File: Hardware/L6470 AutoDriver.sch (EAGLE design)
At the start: 38 parts, among them U1 L6470

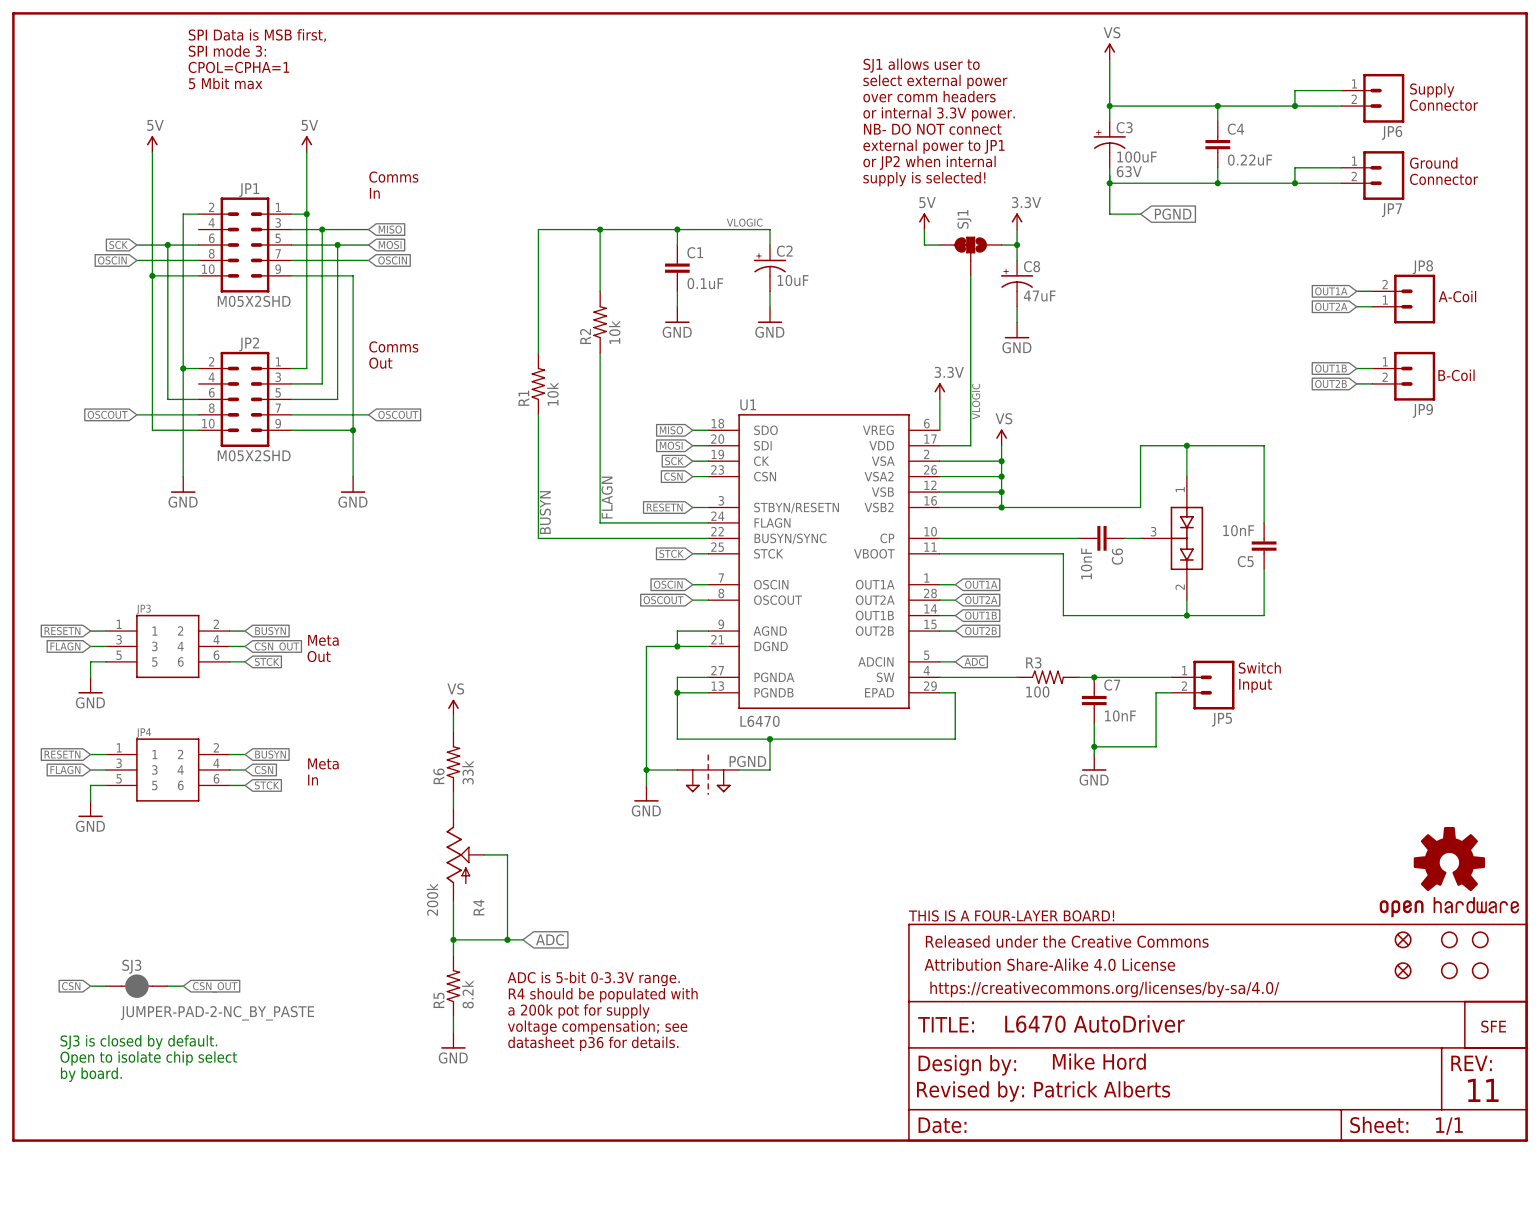
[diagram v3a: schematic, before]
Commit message: Making changes suggest by Pete L
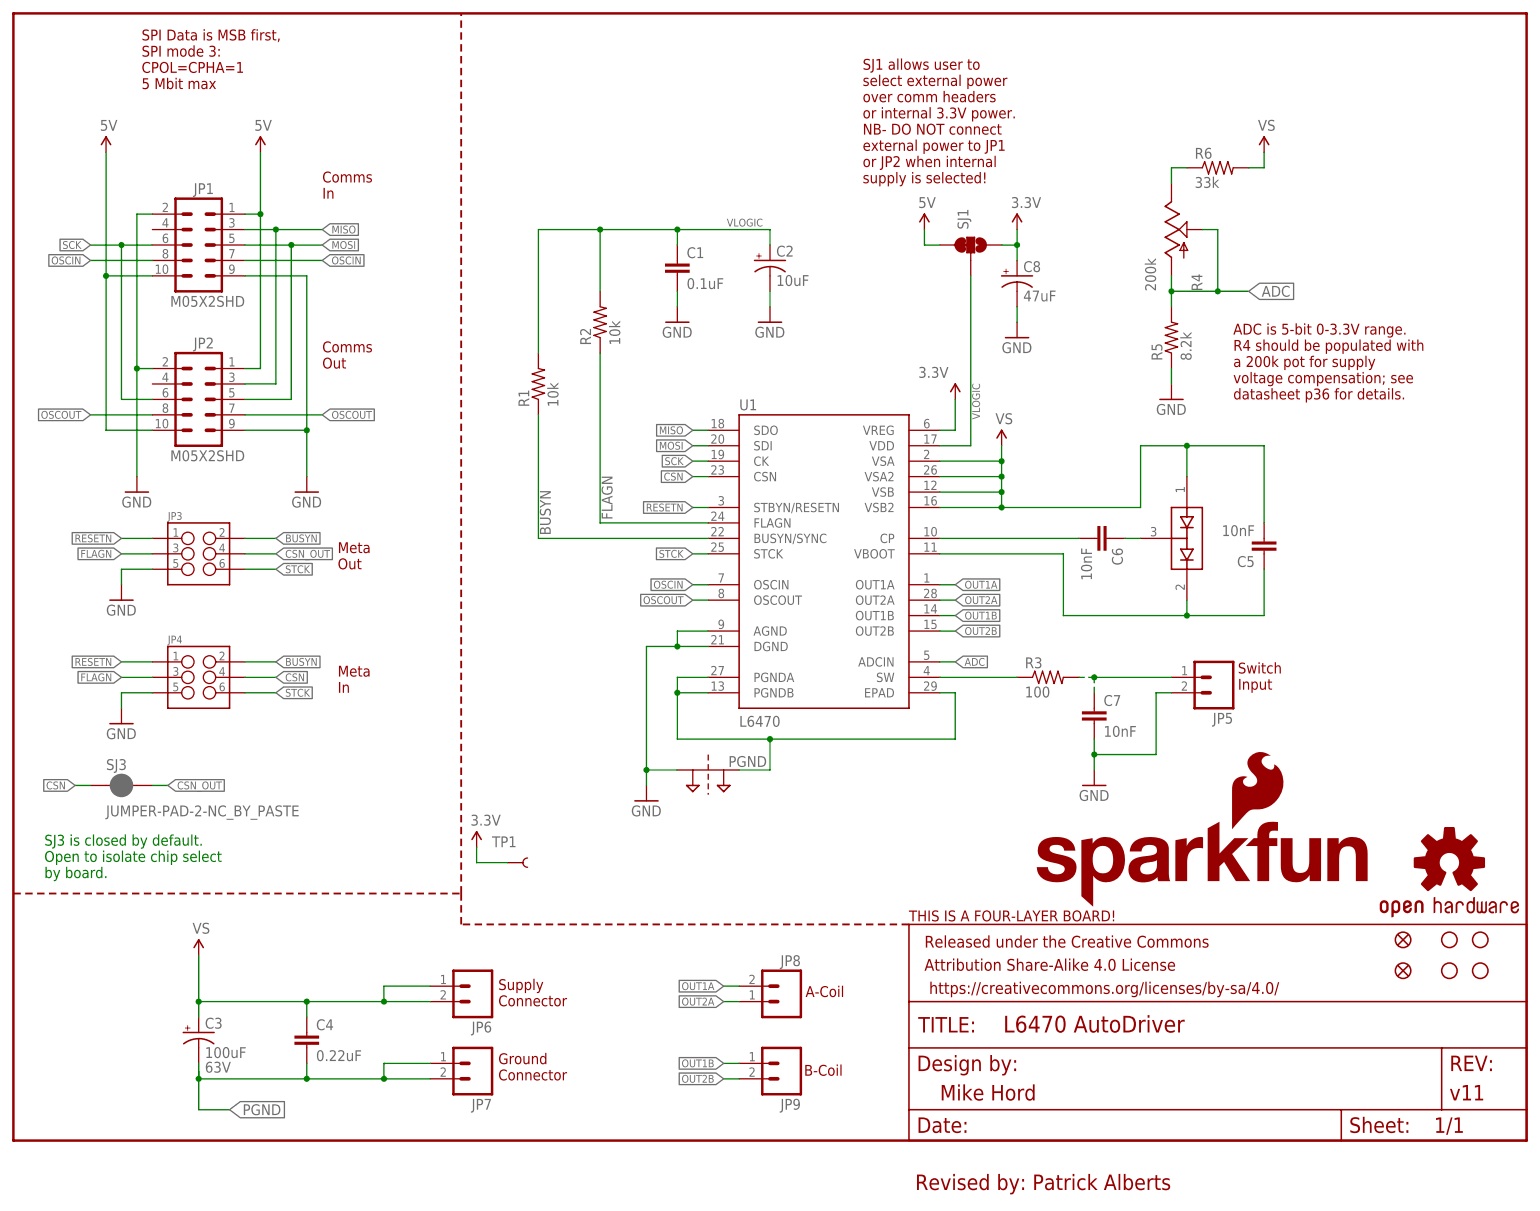
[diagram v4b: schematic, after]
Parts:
- added TP1: TEST-POINTTP_15TH_THRU, SparkFun-Passives:TEST-POINTTP_15TH_THRU
- C3: device SparkFun-Capacitors:CAP_POLD -> SparkFun-Capacitors:100UF-63V-20%(ELECT)
- FRAME1: value FRAME-LETTER -> (none); DESIGNER (none) -> Mike Hord; VERSION (none) -> v11
- JP3, JP4: device SparkFun-Connectors:M03X2 -> SparkFun-Connectors:M03X2SHROUD
- LOGO2: value LOGO-SFENEW -> SFE_LOGO_NAME_FLAME.2_INCH; device SparkFun:LOGO-SFENEW -> SparkFun-Aesthetics:SFE_LOGO_NAME_FLAME.2_INCH
- R4: device SparkFun:POT100K_3362U -> SparkFun-Electromechanical:POT100K_3362U
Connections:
- net 3.3V: now also TP1.1
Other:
- note removed: "11"
- note removed: "Mike Hord"
- moved on the sheet: C3, C4, C7, JP1, JP2, JP6, JP7, JP8, JP9, R4, R5, R6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

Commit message: Fixed more feedback from Pete after 1st proto cam failure
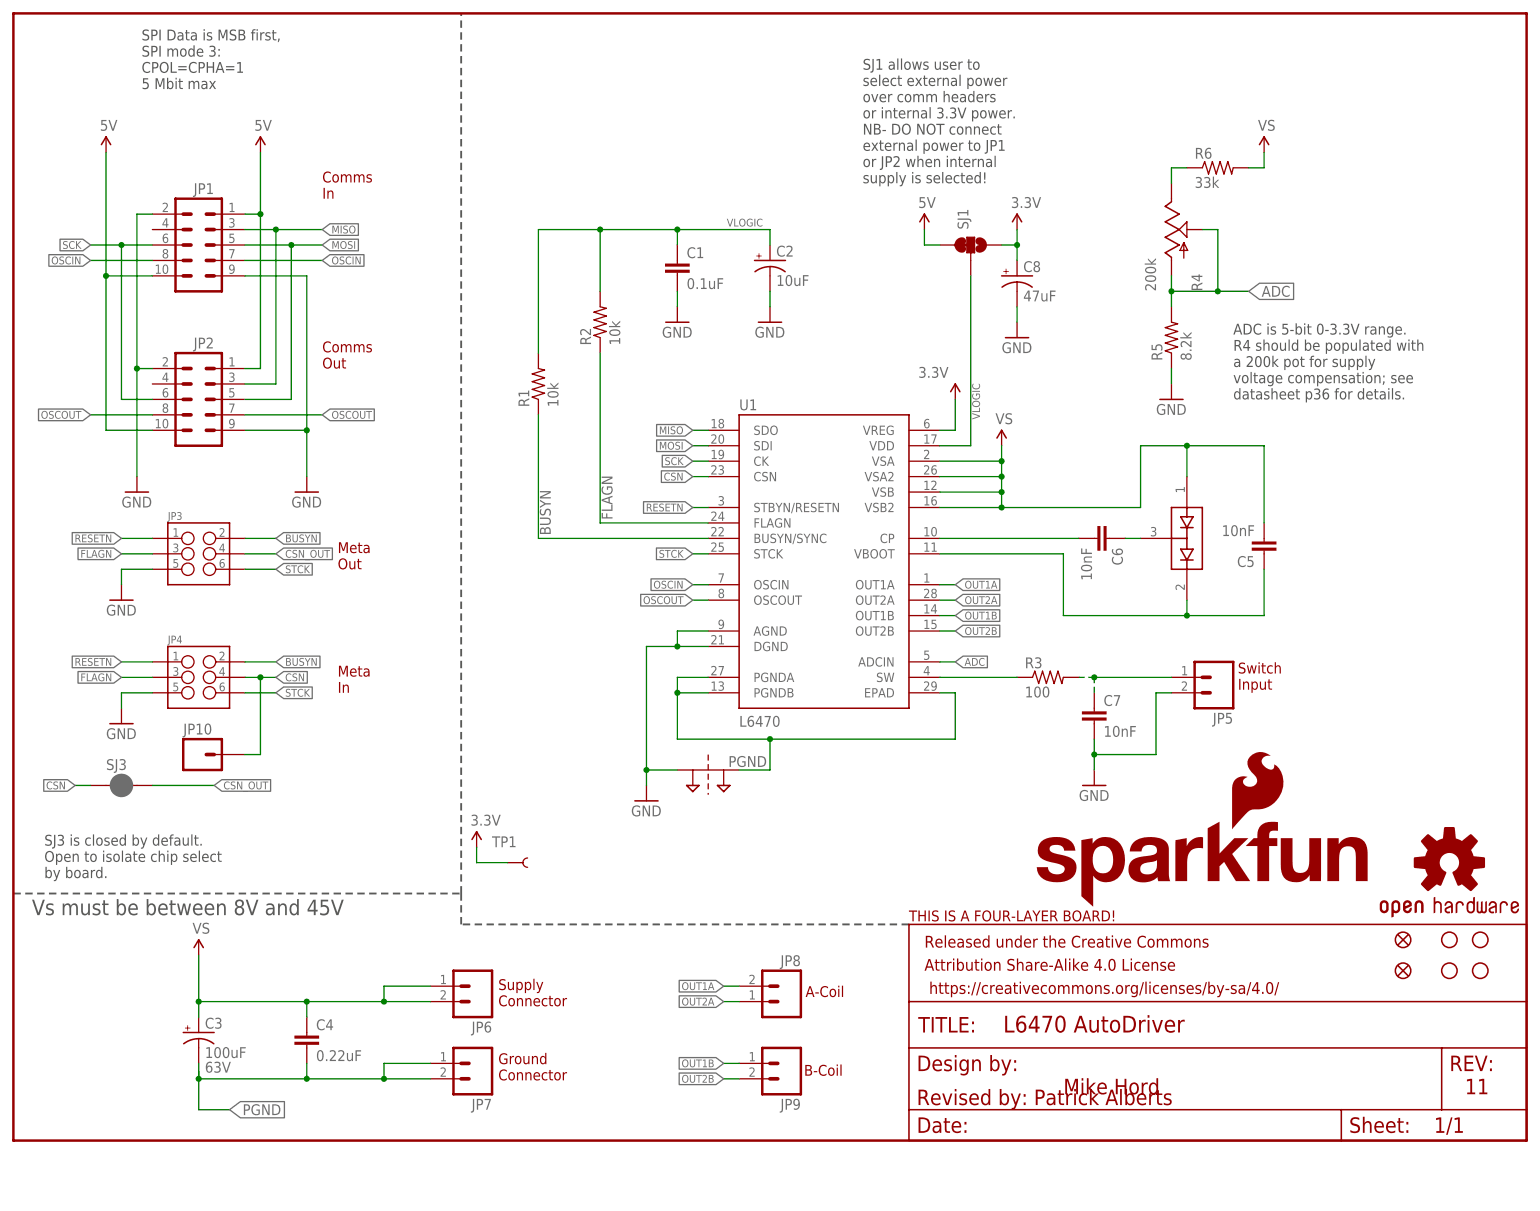
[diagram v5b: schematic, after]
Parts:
- added JP10: (no value), SparkFun-Connectors:M01PTH
- FRAME1: DESIGNER Mike Hord -> (none); VERSION v11 -> (none)
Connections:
- net CSN: now also JP10.1
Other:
- note added: "11"
- note added: "Mike Hord"
- note added: "Vs must be between 8V and 45V"

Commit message: Significant changes from customer feedback:  - now more daisy chainable  - labels changed to make more sense  - Change C5 to 220nF
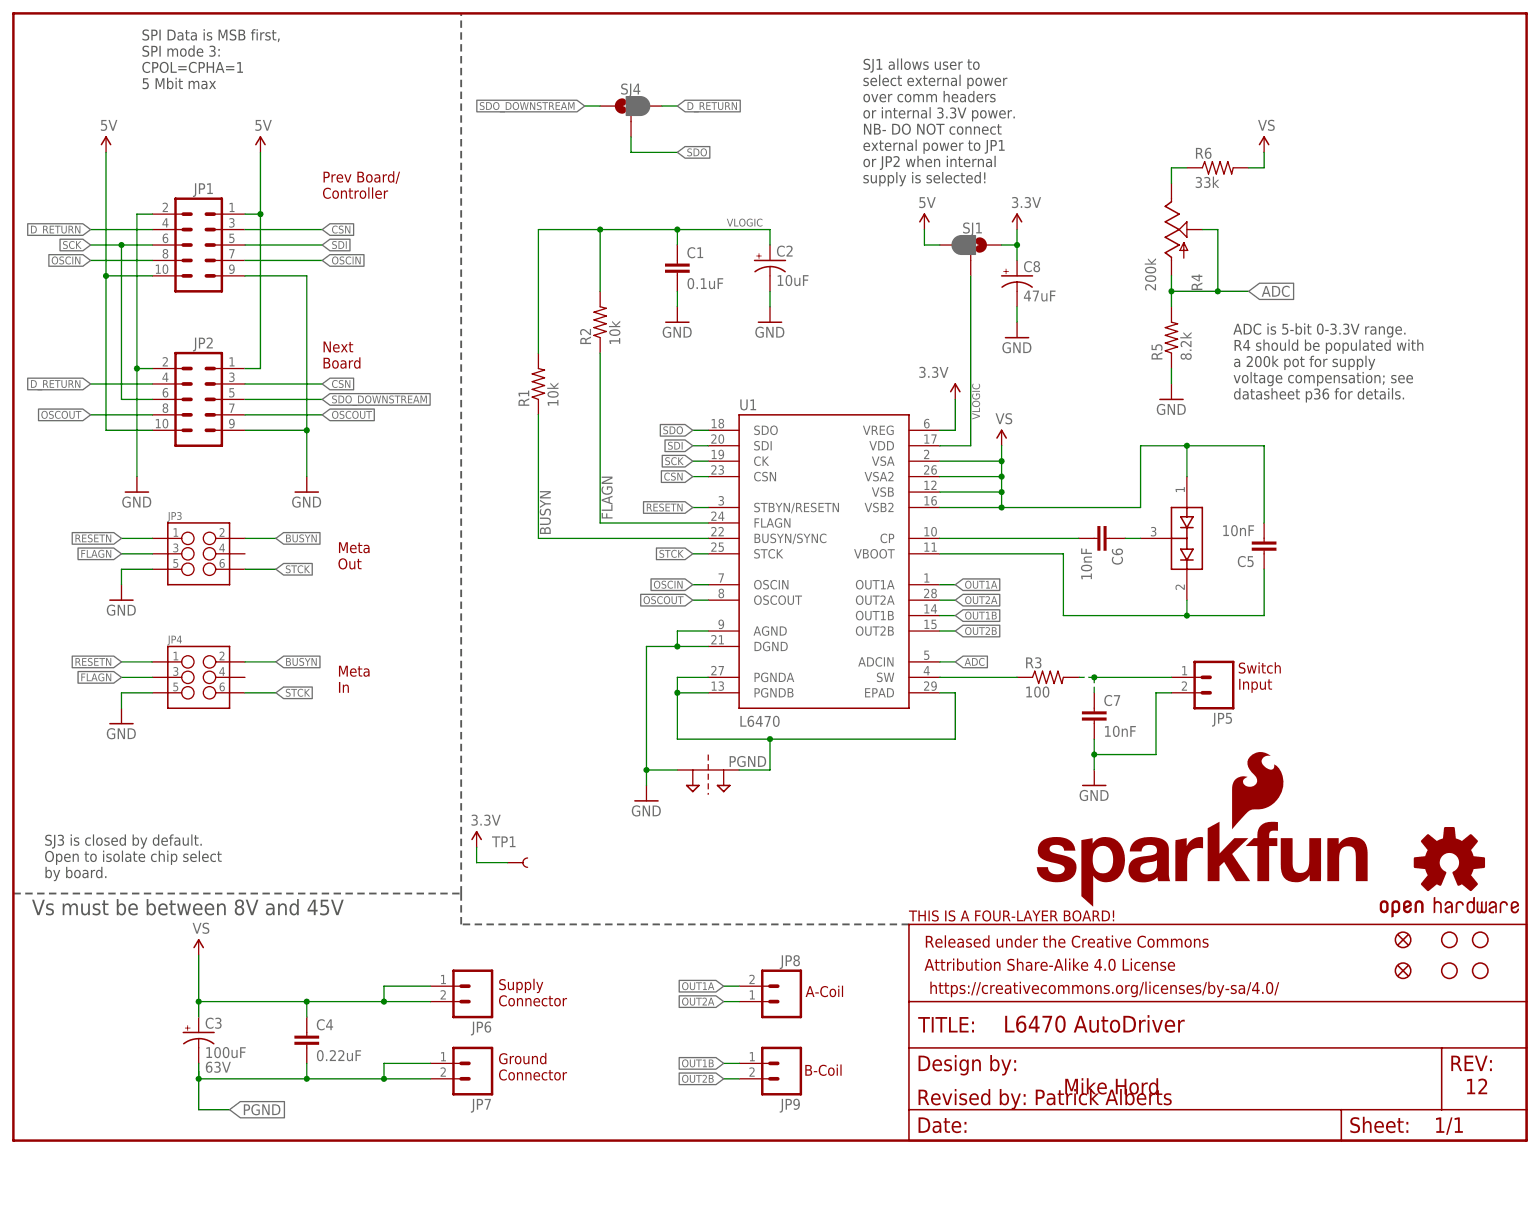
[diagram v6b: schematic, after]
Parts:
- removed JP10: (no value), SparkFun-Connectors:M01PTH
- removed SJ3: JUMPER-PAD-2-NC_BY_PASTE, SparkFun-Passives:JUMPER-PAD-2-NC_BY_PASTE
- added SJ4: JUMPER-PAD-3-2OF3_NC_BY_PASTE, SparkFun-Passives:JUMPER-PAD-3-2OF3_NC_BY_PASTE
- FRAME1: value (none) -> FRAME-LETTER
- SJ1: value (none) -> JUMPER-PAD-3-2OF3_NC_BY_PASTE; device SparkFun-Passives:SOLDERJUMPER_2WAYPASTE1&2 -> SparkFun-Passives:JUMPER-PAD-3-2OF3_NC_BY_PASTE
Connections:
- net N$5 renamed SWITCH_SIG
- net N$6 renamed SWITCH_INPUT
- net N$7 renamed V_CP
- net N$8 renamed CP_HIGH
- net N$9 renamed V_BOOT
- removed net CSN_OUT: JP3.4, SJ3.2
- removed net MISO: JP1.3, JP2.3, U1.SDO
- removed net MOSI: JP1.5, JP2.5, U1.SDI
- new net D_RETURN: JP1.4, JP2.4, SJ4.3
- new net SDI: JP1.5, U1.SDI
- new net SDO: SJ4.2, U1.SDO
- new net SDO_DOWNSTREAM: JP2.5, SJ4.1
- net 3.3V: now also SJ1.1; no longer SJ1.3
- net 5V: now also SJ1.3; no longer SJ1.1
- net CSN: now also JP1.3, JP2.3; no longer JP10.1, JP4.4, SJ3.1
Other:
- note added: "12"
- note added: "Next Board"
- note added: "Prev Board/ Controller"
- note removed: "11"
- note removed: "Comms In"
- note removed: "Comms Out"

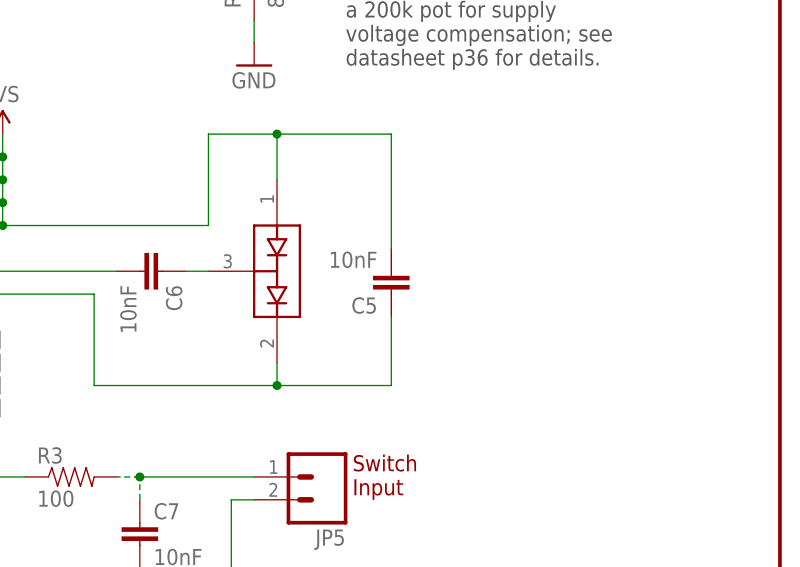
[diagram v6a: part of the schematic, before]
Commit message: Changes from customer feedback:  - now easier to daisy chain!  - labels make more sense in light of daisy chaining  - change C5 to 220nF
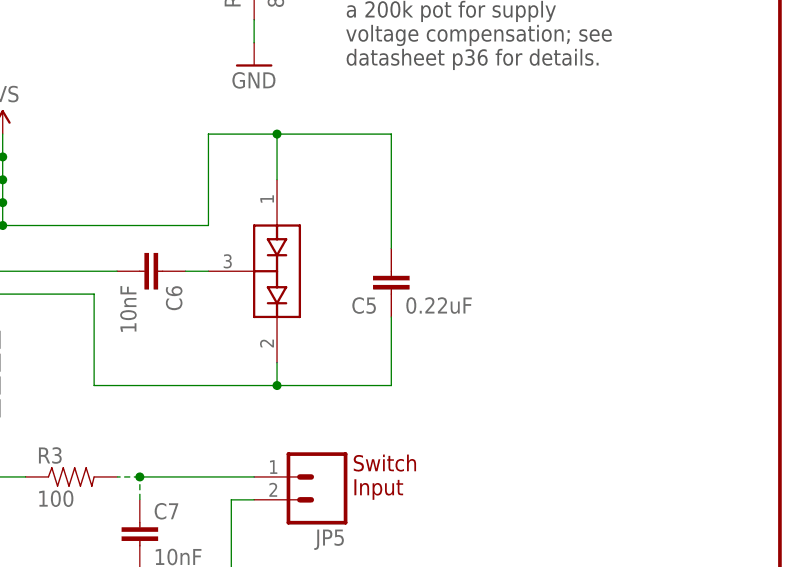
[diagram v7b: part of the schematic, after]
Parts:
- C5: value 10nF -> 0.22uF; device SparkFun-Capacitors:10NF/10000PF-50V-10%(0603) -> SparkFun-Capacitors:0.22UF50V-20%,+80%(0603)
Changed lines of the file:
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@@
 <part name="D1" library="SparkFun-DiscreteSemi" deviceset="BAV99" device="" value="BAV99"/>
 <part name="C6" library="SparkFun-Capacitors" deviceset="10NF/10000PF-50V-10%(0603)" device="" value="10nF"/>
-<part name="C5" library="SparkFun-Capacitors" deviceset="10NF/10000PF-50V-10%(0603)" device="" value="10nF"/>
+<part name="C5" library="SparkFun-Capacitors" deviceset="0.22UF50V-20%,+80%(0603)" device="" value="0.22uF"/>
 <part name="C4" library="SparkFun-Capacitors" deviceset="0.22UF50V-20%,+80%(0603)" device="" value="0.22uF"/>
 <part name="C3" library="SparkFun-Capacitors" deviceset="100UF-63V-20%(ELECT)" device="" value="100uF"/>
@@
 <instance part="D1" gate="G$1" x="193.04" y="99.06" rot="R270"/>
 <instance part="C6" gate="G$1" x="177.8" y="99.06" rot="R270"/>
-<instance part="C5" gate="G$1" x="205.74" y="99.06" rot="R180"/>
+<instance part="C5" gate="G$1" x="205.74" y="99.06" smashed="yes" rot="R180">
+<attribute name="NAME" x="204.216" y="96.139" size="1.778" layer="95" rot="R180"/>
+<attribute name="VALUE" x="207.264" y="94.361" size="1.778" layer="96"/>
+</instance>
 <instance part="C4" gate="G$1" x="48.26" y="15.24"/>
 <instance part="C3" gate="G$1" x="30.48" y="17.78"/>
